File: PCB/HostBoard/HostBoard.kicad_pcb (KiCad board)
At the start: 2 copper layers, 21 parts, among them J1 Conn_01x06, J10 Conn_01x05, J11 Screw_Terminal_01x02, J12 Conn_02x07_Odd_Even, J2 Conn_01x03, J3 Conn_01x06, J4 Conn_01x03, J5 Conn_01x06, J6 Conn_01x04, J7 Conn_01x04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

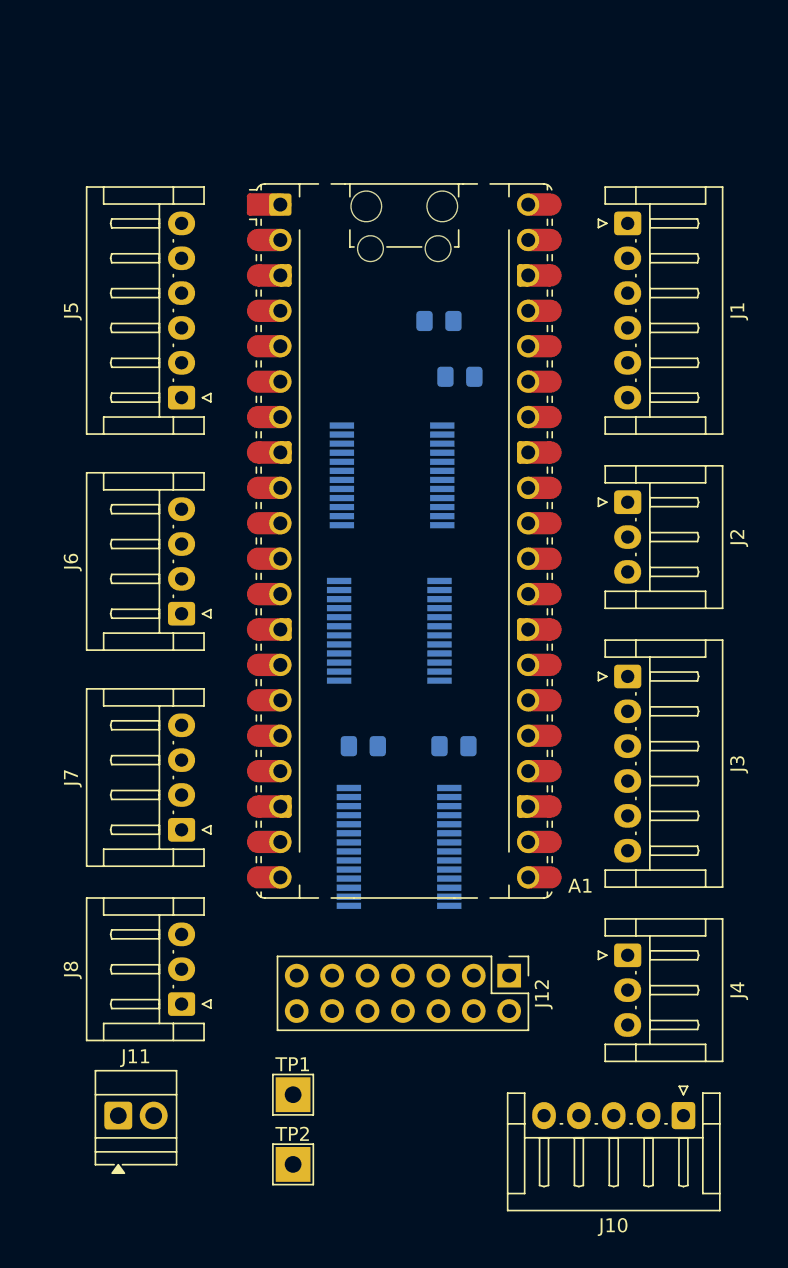
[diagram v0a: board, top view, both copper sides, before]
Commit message: PCB Routing. Signals done except VMot and TPx. Need power planes, silk and outline
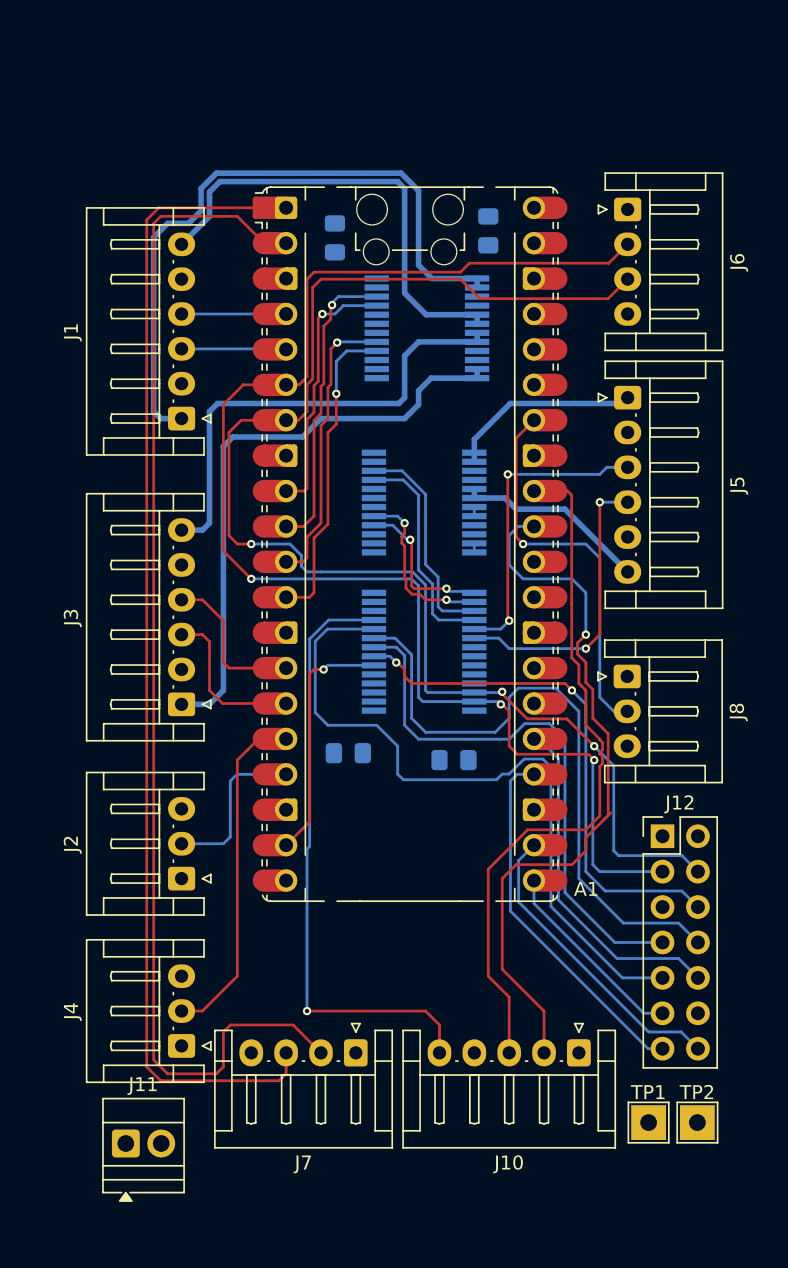
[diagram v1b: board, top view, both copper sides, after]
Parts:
- moved J6 43.2 mm to (143.0, 61.0), turned to -90 degrees
- moved J2 41.9 mm to (111.0, 109.0), turned to 90 degrees
- moved J8 39.7 mm to (143.0, 94.5), turned to -90 degrees
- moved J1 34.9 mm to (111.0, 76.0), turned to 90 degrees
- moved J4 32.7 mm to (111.0, 121.0), turned to 90 degrees
- moved J3 32.1 mm to (111.0, 96.5), turned to 90 degrees
- moved J5 32.0 mm to (143.0, 74.5), turned to -90 degrees
- moved TP2 29.2 mm to (148.0, 126.5)
- moved TP1 25.6 mm to (144.5, 126.5)
- moved J7 20.3 mm to (123.5, 121.5), turned to 180 degrees
- moved J12 14.9 mm to (145.5, 106.0), turned to 0 degrees
- moved U1 14.1 mm to (128.4, 92.7)
- moved U2 10.8 mm to (128.6, 69.5)
- moved C2 10.7 mm to (133.0, 62.5), turned to -90 degrees
- moved C1 9.55 mm to (122.0, 63.0), turned to 90 degrees
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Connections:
- J1 pad 3: Net-(A1-GPIO2) -> Net-(A1-GPIO3)
- J1 pad 4: Net-(A1-GPIO3) -> Net-(A1-GPIO2)
- J3 pad 3: Net-(A1-GPIO10) -> Net-(A1-GPIO11)
- J3 pad 4: Net-(A1-GPIO11) -> Net-(A1-GPIO10)
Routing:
- net SDA_0: track 0.00 -> 99.3 mm, vias 0 -> 3
- net SCL_0: track 0.00 -> 98.1 mm, vias 0 -> 3
- net Net-(A1-GPIO1): track 0.00 -> 85.9 mm
- net Net-(A1-GPIO0): track 0.00 -> 82.4 mm
- net Net-(A1-GPIO26_ADC0): track 0.00 -> 52.1 mm, vias 0 -> 1
- net Net-(J12-Pin_9): track 0.00 -> 50.7 mm
- net Net-(A1-GPIO27_ADC1): track 0.00 -> 49.6 mm
- net Net-(J1-Pin_1): track 0.00 -> 47.7 mm
- net Net-(J12-Pin_8): track 0.00 -> 45.5 mm
- net Net-(J10-Pin_5): track 0.00 -> 43.9 mm, vias 0 -> 1
- net Net-(J3-Pin_1): track 0.00 -> 42.4 mm
- net Net-(J12-Pin_7): track 0.00 -> 39.8 mm
- net Net-(J12-Pin_6): track 0.00 -> 38.0 mm, vias 0 -> 2
- net Net-(J3-Pin_6): track 0.00 -> 33.9 mm
- net Net-(J1-Pin_6): track 0.00 -> 33.1 mm
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
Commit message: Completed PCB for existing schematic, need to re-assign LCD and check schematic
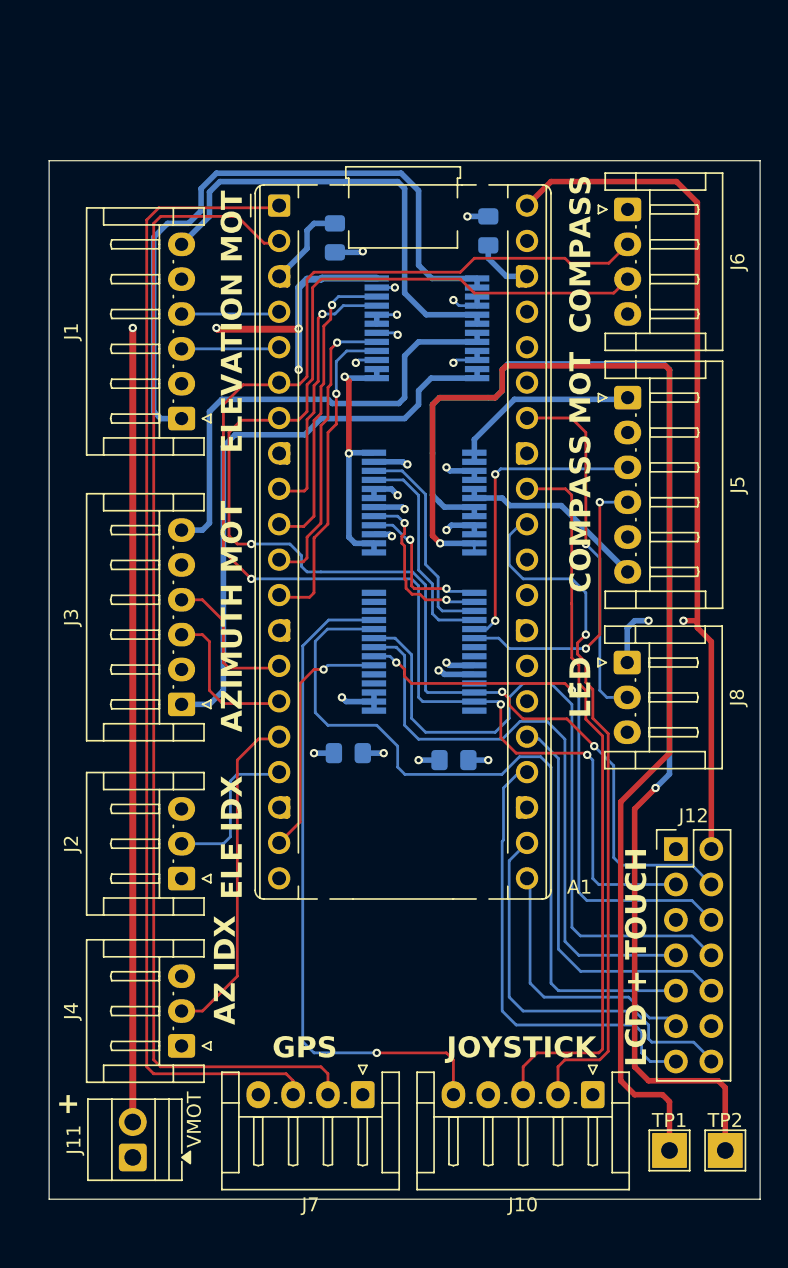
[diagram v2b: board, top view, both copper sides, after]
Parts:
- A1: footprint Module:RaspberryPi_Pico_Common_Unspecified -> Module:RaspberryPi_Pico_Common_THT
- moved A1 26.0 mm to (118.0, 60.7)
- moved J10 3.16 mm to (140.5, 124.5)
- moved J7 3.04 mm to (124.0, 124.5)
- moved TP2 2.83 mm to (150.0, 128.5)
- moved TP1 2.50 mm to (146.0, 128.5)
- moved J12 1.33 mm to (146.5, 106.9)
- moved J11 1.12 mm to (107.5, 129.0), turned to 90 degrees
- moved J8 1.00 mm to (143.0, 93.5)
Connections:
- J11 pad 1: Vmotor -> GND
- J11 pad 2: GND -> Vmotor
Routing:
- net Vmotor: track 0.00 -> 106.6 mm, vias 0 -> 6
- net Net-(TP1-Pad1): track 0.65 -> 92.6 mm, vias 0 -> 1
- net Net-(TP2-Pad1): track 0.65 -> 92.4 mm, vias 0 -> 1
- net +5V: track 0.00 -> 68.1 mm, vias 0 -> 2
- net GND: track 0.00 -> 34.3 mm, vias 0 -> 10
- net +3.3V: track 0.00 -> 20.2 mm, vias 0 -> 11
- net Net-(A1-GPIO18): track 26.2 -> 33.5 mm
- net Net-(A1-GPIO17): track 21.8 -> 28.7 mm
- net Net-(A1-GPIO16): track 14.1 -> 19.3 mm
- net Net-(J10-Pin_5): track 43.9 -> 48.1 mm
- net Net-(J12-Pin_9): track 50.7 -> 54.8 mm
- net Net-(J12-Pin_8): track 45.5 -> 49.4 mm
- net Net-(J12-Pin_7): track 39.8 -> 43.3 mm
- net Net-(A1-GPIO19): track 25.4 -> 28.5 mm
- net Net-(A1-GPIO27_ADC1): track 49.6 -> 52.3 mm
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- added copper zone on In2.Cu, net +3.3V
- added copper zone on In1.Cu, net GND
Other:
- board outline added: 51 x 74.5 mm
- copper layers 2 -> 4
- board text added: "+"
- board text added: "AZ IDX"
- board text added: "AZIMUTH MOT"
- board text added: "COMPASS"
- board text added: "COMPASS MOT"
- board text added: "ELE IDX"
- board text added: "ELEVATION MOT"
- board text added: "GPS"
- board text added: "JOYSTICK"
- board text added: "LCD + TOUCH"
- board text added: "LED"
- board text added: "VMOT"

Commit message: Moved TFT_DC and Expander INTA pins to match code
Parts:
- removed TP2: TestPoint, TestPoint:TestPoint_THTPad_2.5x2.5mm_Drill1.2mm
- added J9: Conn_01x03, Connector_PinHeader_2.54mm:PinHeader_1x03_P2.54mm_Vertical, F.Cu at (149.0, 120.5)
- added TP3: TestPoint, TestPoint:TestPoint_Pad_1.0x1.0mm, B.Cu at (130.5, 106.5)
- added TP4: TestPoint, TestPoint:TestPoint_Pad_1.0x1.0mm, B.Cu at (132.5, 108.0)
- TP1: footprint TestPoint:TestPoint_THTPad_2.5x2.5mm_Drill1.2mm -> Connector_PinHeader_2.54mm:PinHeader_1x01_P2.54mm_Vertical; moved to B.Cu
- moved TP1 48.7 mm to (138.0, 80.5), turned to 180 degrees
- moved U2 7.65 mm to (127.1, 62.0)
- moved A1 7.65 mm to (116.5, 53.2)
- moved C1 7.65 mm to (120.5, 55.5)
- moved C2 7.65 mm to (131.5, 55.0)
- moved C3 7.65 mm to (129.0, 93.0)
- moved C4 7.65 mm to (121.5, 92.5)
- moved J1 7.65 mm to (109.5, 68.5)
- moved J10 7.65 mm to (139.0, 117.0)
- moved J11 7.65 mm to (106.0, 121.5)
- moved J2 7.65 mm to (109.5, 101.5)
- moved J3 7.65 mm to (109.5, 89.0)
- moved J4 7.65 mm to (109.5, 113.5)
- moved J5 7.65 mm to (141.5, 67.0)
- moved J6 7.65 mm to (141.5, 53.5)
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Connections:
- net Net-(A1-GPIO0) renamed /TX
- net Net-(A1-GPIO1) renamed /RX
- net Net-(A1-GPIO10) renamed /AZIMUTH_CHA
- net Net-(A1-GPIO11) renamed /AZIMUTH_CHB
- net Net-(A1-GPIO12) renamed /ELEVATION_IDX
- net Net-(A1-GPIO13) renamed /AZIMUTH_IDX
- net Net-(A1-GPIO16) renamed /TFT_MISO
- net Net-(A1-GPIO17) renamed /TFT_CS
- net Net-(A1-GPIO18) renamed /TFT_SCK
- net Net-(A1-GPIO19) renamed /TFT_MOSI
- net Net-(A1-GPIO2) renamed /ELEVATION_CHA
- net Net-(A1-GPIO26_ADC0) renamed /JOY_Y
- net Net-(A1-GPIO27_ADC1) renamed /JOY_X
- net Net-(A1-GPIO28_ADC2) renamed /JOY_SW
- net Net-(A1-GPIO3) renamed /ELEVATION_CHB
- net Net-(A1-GPIO6) renamed /ELEVATION_FWD
- net Net-(A1-GPIO7) renamed /ELEVATION_REV
- net Net-(A1-GPIO8) renamed /AZIMUTH_FWD
- net Net-(A1-GPIO9) renamed /AZIMUTH_REV
- A1 pad 19: Net-(A1-GPIO14) -> unconnected-(A1-GPIO14-Pad19)
- A1 pad 26: unconnected-(A1-GPIO20-Pad26) -> /TFT_DC
- A1 pad 27: unconnected-(A1-GPIO21-Pad27) -> /EXP_INT_A
- A1 pad 29: unconnected-(A1-GPIO22-Pad29) -> /SD_CD
- A1 pad 33: GND -> unconnected-(A1-AGND-Pad33)
- J12 pad 12: unconnected-(J12-Pin_12-Pad12) -> /TFT_DC
- TP1 pad 1: Net-(TP1-Pad1) -> /SD_CD
- U1 pad 18: unconnected-(U1-~{RESET}-Pad18) -> +3.3V
- U1 pad 20: Net-(A1-GPIO14) -> /EXP_INT_A
- U3 pad 11: Net-(TP1-Pad1) -> Net-(J9-Pin_2)
- U3 pad 12: Net-(TP1-Pad1) -> Net-(J9-Pin_2)
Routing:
- net Net-(J9-Pin_2): track 0.00 -> 93.4 mm, vias 0 -> 1
- net Net-(TP1-Pad1): track 92.6 -> 0.00 mm, vias 1 -> 0
- net +5V: track 68.1 -> 92.4 mm
- net /EXP_INT_A: track 0.00 -> 22.3 mm, vias 0 -> 1
- net SDA_0: track 101.4 -> 122.9 mm
- net SCL_0: track 99.7 -> 119.2 mm
- net Net-(A1-GPIO14): track 17.9 -> 0.00 mm, vias 1 -> 0
- net /TFT_SCK: track 33.5 -> 16.3 mm, vias 0 -> 2
- net /TFT_CS: track 28.7 -> 11.7 mm, vias 0 -> 1
- net Net-(J12-Pin_7): track 43.3 -> 55.8 mm, vias 0 -> 2
- net /TFT_MOSI: track 28.5 -> 21.7 mm
- net /TFT_MISO: track 19.3 -> 14.3 mm, vias 0 -> 1
- net Net-(J12-Pin_9): track 54.8 -> 50.5 mm
- net /SD_CD: track 0.00 -> 3.99 mm
- net Net-(J12-Pin_6): track 40.5 -> 43.9 mm
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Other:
- board size 51 x 74.5 mm -> 51 x 77 mm
- board text added: "-"
- board text added: "SCL"
- board text added: "SDA"
- board text added: "SD_CD"
